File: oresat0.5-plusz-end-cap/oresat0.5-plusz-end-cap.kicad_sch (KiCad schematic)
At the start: 35 parts, among them J2 U.FL-R-SMA, U1 LTC4305, U2 MMC5883MA, U3 MMC5883MA

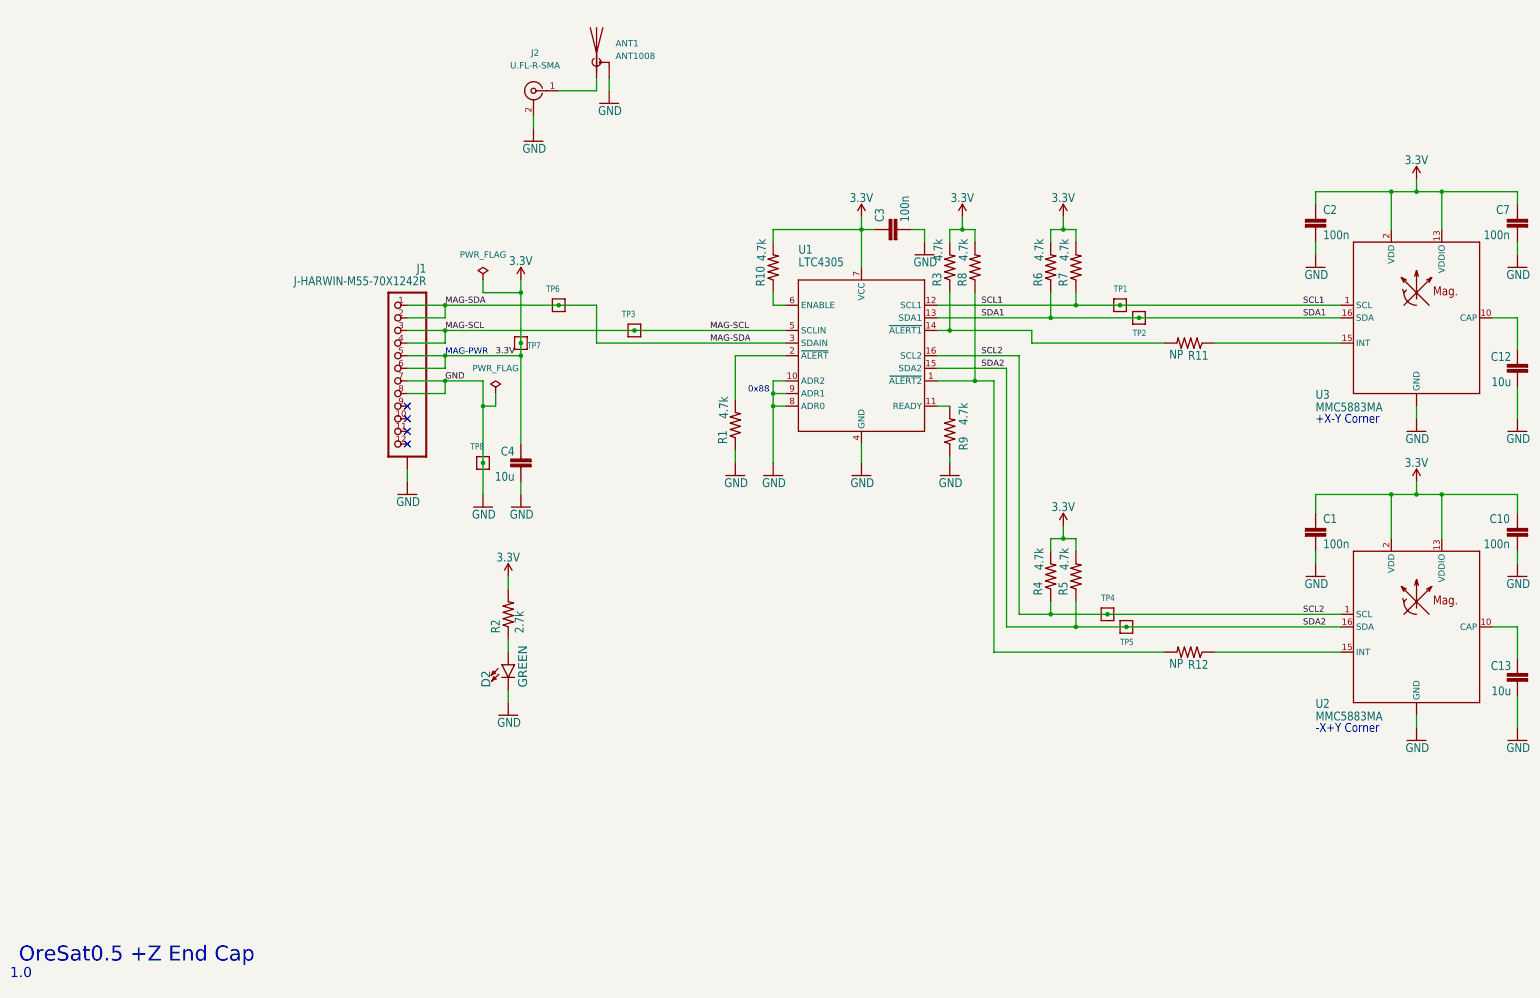
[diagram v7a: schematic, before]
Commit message: Upgrades OreSat0.5 +Z End Cap to v1.2 -- fits the new deployer, and cleans up a bunch of library issues.
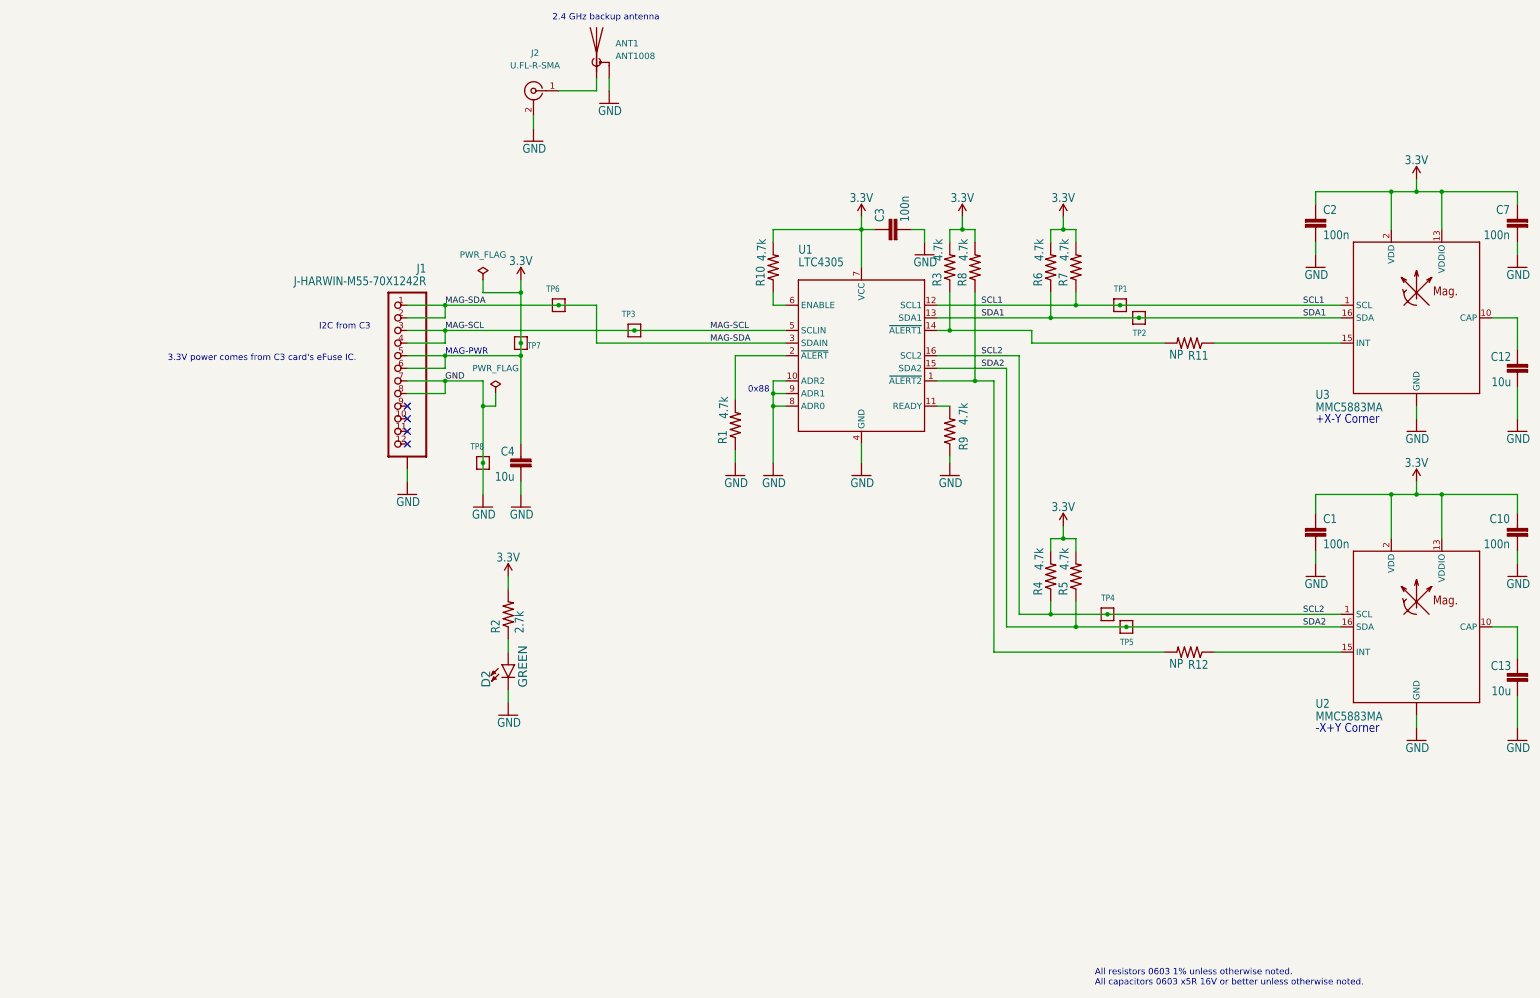
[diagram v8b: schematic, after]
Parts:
- D2: footprint oresat0-plusz-end-cap:LED-0603 -> oresat0.5-plusz-end-cap:LED-0603
- U1: footprint oresat0-plusz-end-cap:16-SSOP -> oresat0.5-plusz-end-cap:16-SSOP
- U2, U3: footprint oresat0-plusz-end-cap:LGA-16(3X3) -> oresat0.5-plusz-end-cap:LGA-16(3X3)
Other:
- note added: "2.4 GHz backup antenna"
- note added: "3.3V power comes from C3 card's eFuse IC."
- note added: "All resistors 0603 1% unless otherwise noted. All capacitors 0603 x5R 16V or better unless otherwise noted."
- note added: "I2C from C3"
- note removed: "1.0"
- note removed: "OreSat0.5 +Z End Cap"
- title: (none) -> OreSat0.5 +Z End Cap
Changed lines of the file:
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@@
 (kicad_sch (version 20230121) (generator eeschema)
   (paper "B")
+  (title_block
+    (title "OreSat0.5 +Z End Cap")
+    (date "2023-12-20")
+    (rev "1.1")
+  )
   (junction (at 231.14 171.45) (diameter 0) (color 0 0 0 0)
   )
@@
     (effects (font (size 1.778 1.5113)) (justify left bottom))
   )
+  (text "3.3V power comes from C3 card's eFuse IC." (at 50.8 135.89 0)
+    (effects (font (size 1.27 1.27)) (justify left bottom))
+  )
   (text "MAG-PWR" (at 106.68 134.62 0)
     (effects (font (size 1.27 1.27)) (justify left bottom))
   )
-  (text "1.0" (at 19.045 260.231 0)
-    (effects (font (size 2.032 2.032)) (justify left bottom))
-  )
-  (text "OreSat0.5 +Z End Cap" (at 20.8209 257.0409 0)
-    (effects (font (size 3.048 3.048)) (justify left bottom))
+  (text "All resistors 0603 1% unless otherwise noted.\nAll capacitors 0603 x5R 16V or better unless otherwise noted."
+    (at 237.49 261.62 0)
+    (effects (font (size 1.27 1.27)) (justify left bottom))
   )
   (text "+X-Y Corner" (at 281.94 148.59 0)
     (effects (font (size 1.778 1.5113)) (justify left bottom))
   )
+  (text "I2C from C3" (at 81.28 129.54 0)
+    (effects (font (size 1.27 1.27)) (justify left bottom))
+  )
+  (text "2.4 GHz backup antenna" (at 128.27 67.31 0)
+    (effects (font (size 1.27 1.27)) (justify left bottom))
+  )
   (label "SDA1" (at 279.4 127 0) (fields_autoplaced)
     (effects (font (size 1.2446 1.2446)) (justify left bottom))
@@
     (effects (font (size 1.2446 1.2446)) (justify left bottom))
   )
-  (label "3.3V" (at 116.84 134.62 0) (fields_autoplaced)
-    (effects (font (size 1.2446 1.2446)) (justify left bottom))
-  )
   (label "SDA1" (at 214.63 127 0) (fields_autoplaced)
     (effects (font (size 1.2446 1.2446)) (justify left bottom))
@@
       (effects (font (size 1.778 1.778)) (justify left top))
     )
-    (property "Footprint" "oresat0-plusz-end-cap:LED-0603" (at 119.38 196.85 0)
+    (property "Footprint" "oresat0.5-plusz-end-cap:LED-0603" (at 119.38 196.85 0)
       (effects (font (size 1.27 1.27)) hide)
     )
@@
       (effects (font (size 1.778 1.5113)) (justify left bottom))
     )
-    (property "Footprint" "oresat0-plusz-end-cap:LGA-16(3X3)" (at 302.26 127 0)
-      (effects (font (size 1.27 1.27)) hide)
-    )
-    (property "Datasheet" "" (at 302.26 127 0)
+    (property "Footprint" "oresat0.5-plusz-end-cap:LGA-16(3X3)" (at 302.26 127 0)
+      (effects (font (size 1.27 1.27)) hide)
+    )
+    (property "Datasheet" "https://mm.digikey.com/Volume0/opasdata/d220001/medias/docus/2326/MMC5883MA_RevC_4--28-17.pdf" (at 302.26 127 0)
       (effects (font (size 1.27 1.27)) hide)
     )
@@
       (effects (font (size 1.778 1.5113)) (justify left bottom))
     )
-    (property "Footprint" "oresat0-plusz-end-cap:LGA-16(3X3)" (at 302.26 189.23 0)
-      (effects (font (size 1.27 1.27)) hide)
-    )
-    (property "Datasheet" "" (at 302.26 189.23 0)
+    (property "Footprint" "oresat0.5-plusz-end-cap:LGA-16(3X3)" (at 302.26 189.23 0)
+      (effects (font (size 1.27 1.27)) hide)
+    )
+    (property "Datasheet" "https://mm.digikey.com/Volume0/opasdata/d220001/medias/docus/2326/MMC5883MA_RevC_4--28-17.pdf" (at 302.26 189.23 0)
       (effects (font (size 1.27 1.27)) hide)
     )
@@
       (effects (font (size 1.778 1.5113)) (justify left bottom))
     )
-    (property "Footprint" "oresat0-plusz-end-cap:16-SSOP" (at 190.5 134.62 0)
-      (effects (font (size 1.27 1.27)) hide)
-    )
-    (property "Datasheet" "" (at 190.5 134.62 0)
-      (effects (font (size 1.27 1.27)) hide)
-    )
+    (property "Footprint" "oresat0.5-plusz-end-cap:16-SSOP" (at 190.5 134.62 0)
+      (effects (font (size 1.27 1.27)) hide)
+    )
+    (property "Datasheet" "https://www.analog.com/media/en/technical-documentation/data-sheets/4305.pdf" (at 190.5 134.62 0)
+      (effects (font (size 1.27 1.27)) hide)
+    )
